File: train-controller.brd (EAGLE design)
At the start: 75.9 x 21.7 mm, 19 parts, among them IC1 MCP4131, IC2 L272, Q1 2n3906, Q2 2n2222

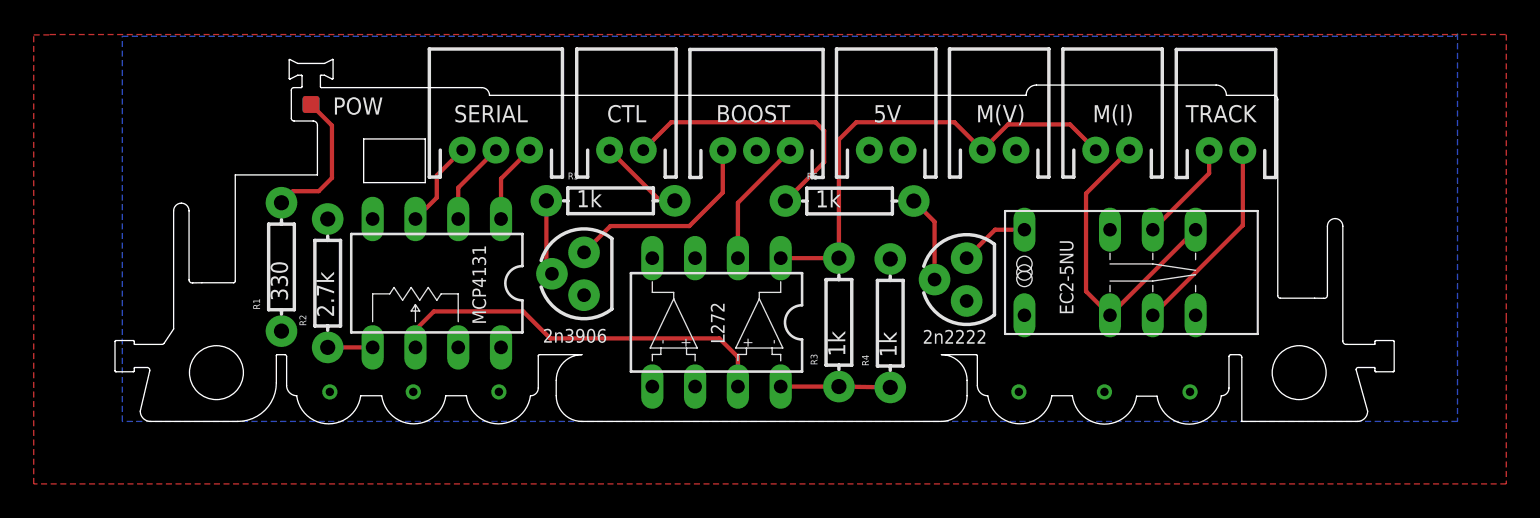
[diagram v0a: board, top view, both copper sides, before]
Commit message: board v2, adding readme and license
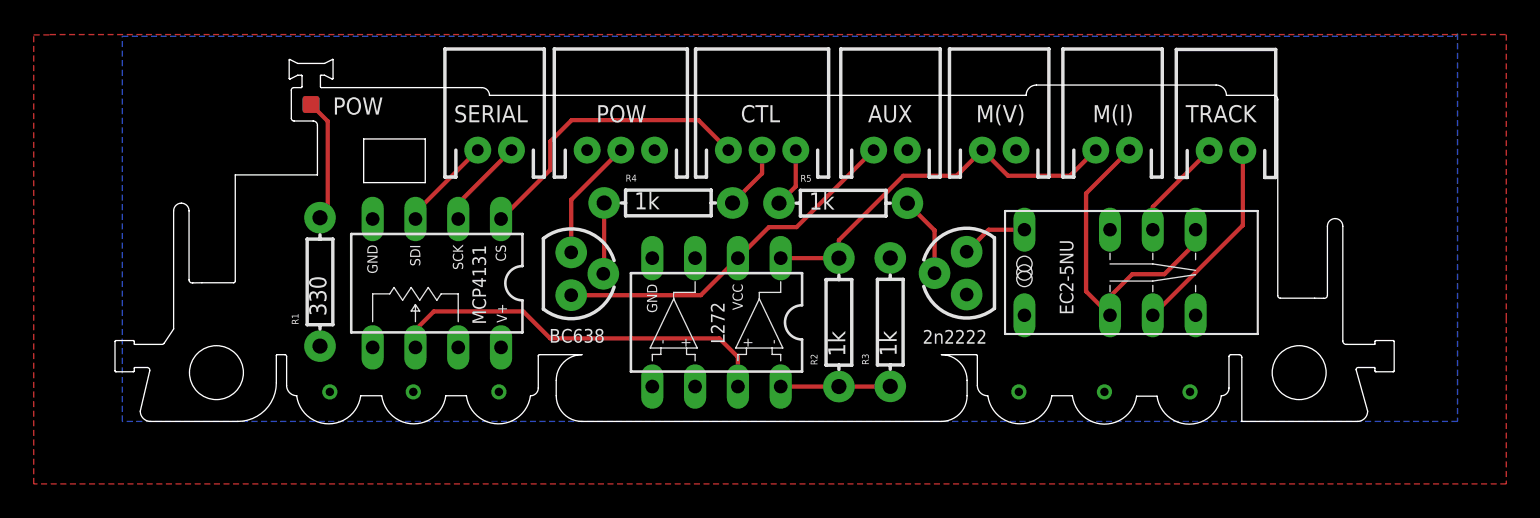
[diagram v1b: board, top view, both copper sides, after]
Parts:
- removed 5V: M02, custom-parts:JST-2-PTH
- removed BOOST: M03, custom-parts:JST-3-PTH
- removed R6: 1k, SparkFun-Resistors:AXIAL-0.3
- added AUX: M02, custom-parts:JST-2-PTH
- added POW: M03, custom-parts:JST-3-PTH
- CTL: value M02 -> M03; device custom-parts:JST-2-PTH -> custom-parts:JST-3-PTH
- Q1: value 2n3906 -> BC838
- R2: value 2.7k -> 1k
- SERIAL: value M03 -> M02; device custom-parts:JST-3-PTH -> custom-parts:JST-2-PTH
- moved R2 30.4 mm to (42.5, 6.03)
- moved R4 15.0 mm to (32.4, 13.1), turned to 0 degrees
- moved R5 13.8 mm to (42.8, 13.1)
- moved CTL 8.05 mm to (38.0, 16.3)
- moved R3 3.05 mm to (45.6, 6.05)
- moved R1 2.45 mm to (11.7, 8.43)
- moved Q1 0.76 mm to (26.6, 8.92), turned to 270 degrees
- moved Q2 0.38 mm to (50.1, 8.95)
- moved SERIAL 0.08 mm to (22.1, 16.3)
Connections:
- removed net 5V-EN: BOOST.1, Q1.3
- removed net N$2: IC1.A, R2.P$1
- new net 12V-EN: AUX.1, IC2.V+, Q1.3
- net 12V: now also POW.2, Q1.1; no longer BOOST.3, IC2.V+
- net 5V: now also IC1.B, POW.1; no longer 5V.1, Q1.1, R2.P$2
- net CS: now also CTL.1; no longer SERIAL.3
- net DIR: now also CTL.3, R5.P$1; no longer CTL.2, R6.P$1
- net EN: now also CTL.2, R4.P$2; no longer CTL.1, R5.P$2
- net GND: now also AUX.2, IC1.A, POW.3, R3.P$2; no longer 5V.2, BOOST.2, IC1.B, R4.P$2
- net N$1: now also R4.P$1; no longer R5.P$1
- net N$3: now also R2.P$1; no longer R4.P$1
- net N$6: now also R5.P$2; no longer R6.P$2
- net POW: now also R2.P$2; no longer R3.P$2
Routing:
- net 12V-EN: track 0.00 -> 21.5 mm
- net DIR: track 16.7 -> 3.56 mm
- net CS: track 4.79 -> 17.6 mm
- net 5V-EN: track 12.2 -> 0.00 mm
- net POW: track 28.1 -> 23.2 mm
- net N$2: track 2.67 -> 0.00 mm
- net EN: track 5.12 -> 3.86 mm
- net N$19: track 8.48 -> 7.32 mm
- net N$7: track 18.6 -> 19.8 mm
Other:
- board text added: "AUX"
- board text added: "BC638"
- board text removed: "2n3906"
- board text removed: "5V"
- board text removed: "BOOST"

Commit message: addressing several items from the bug/feature list
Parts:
- removed Q2: 2n2222, custom-parts:TO-92
- added D1: (no value), SparkFun-DiscreteSemi:DIODE-1N4148
- added Q3: BC638, custom-parts:TO-92
- Q1: value BC838 -> BC638
- moved POW 8.51 mm to (38.1, 16.3)
- moved CTL 8.38 mm to (29.6, 16.3)
- moved S1 1.14 mm to (60.4, 10.0)
- moved R4 0.89 mm to (31.5, 13.1)
- moved R5 0.25 mm to (42.5, 13.1)
- moved Q1 0.13 mm to (26.5, 8.92)
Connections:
- removed net N$5: Q2.3, S1.-
- new net N$2: D1.C, Q3.3, S1.+
- net 12V: now also POW.3; no longer POW.2
- net 5V: now also Q3.1; no longer S1.+
- net EN: now also R4.P$1; no longer R4.P$2
- net GND: now also D1.A, M(V).1, POW.2, S1.-; no longer M(V).2, POW.3, Q2.1
- net N$1: now also R4.P$2; no longer R4.P$1
- net N$6: now also Q3.2; no longer Q2.2
- net POW: now also M(V).2; no longer M(V).1
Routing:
- net DIR: track 3.56 -> 17.9 mm
- net CS: track 17.6 -> 6.81 mm
- net 12V: track 7.29 -> 16.1 mm
- net N$2: track 0.00 -> 8.25 mm
- net N$1: track 4.22 -> 8.92 mm
- net N$5: track 3.97 -> 0.00 mm
- net N$6: track 4.82 -> 8.25 mm
- net N$7: track 19.8 -> 18.3 mm
- net RIGHT: track 6.08 -> 4.86 mm
- net LEFT: track 12.0 -> 10.8 mm
- net 12V-EN: track 21.5 -> 22.4 mm
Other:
- board text removed: "2n2222"

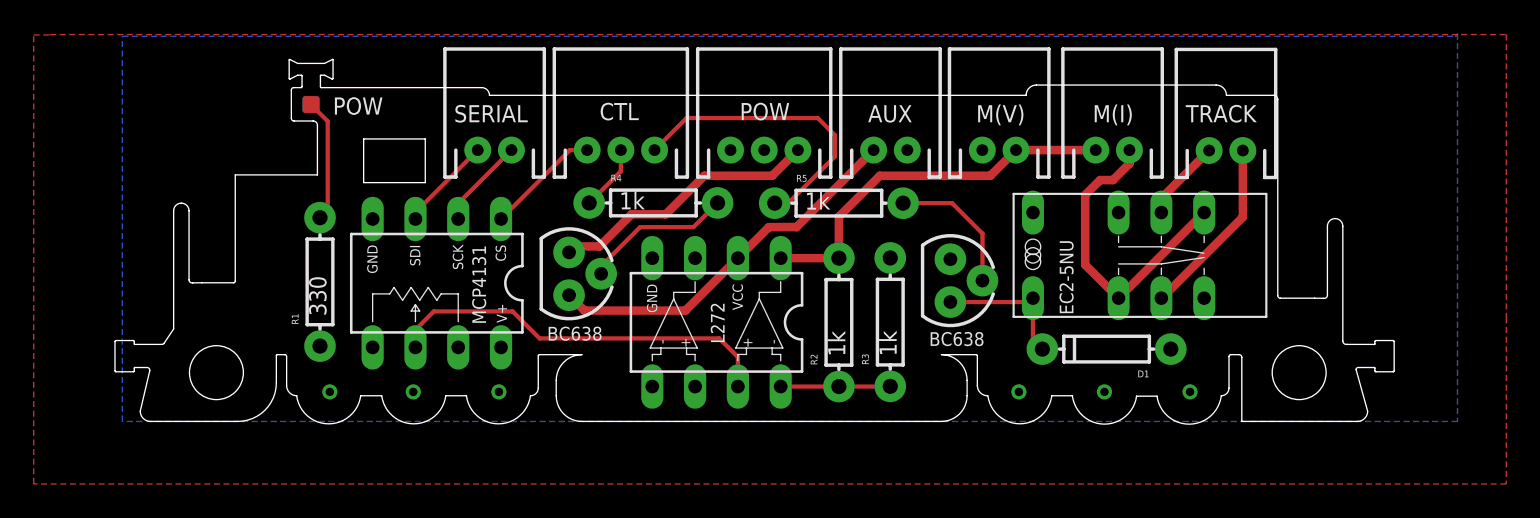
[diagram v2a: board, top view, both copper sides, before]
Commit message: adding controller board
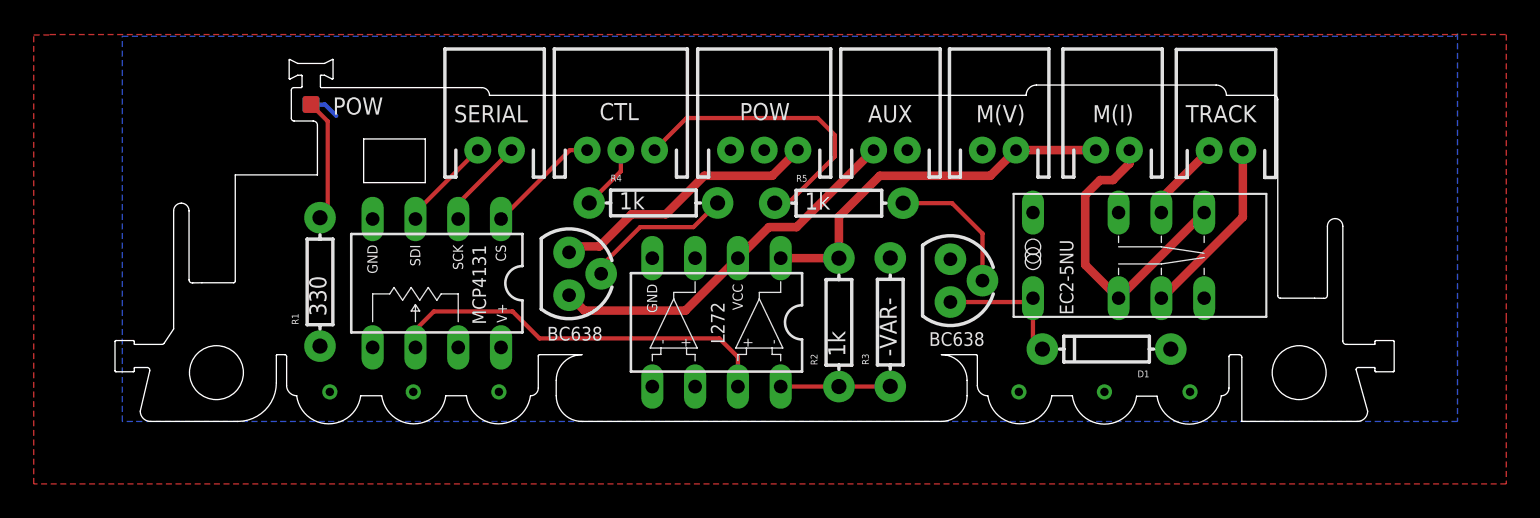
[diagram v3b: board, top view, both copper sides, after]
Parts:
- R3: value 1k -> -VAR-
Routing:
- net GND: track 0.00 -> 1.78 mm
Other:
- board text added: "Branding Goes Here V1 underdogma.net/trains"
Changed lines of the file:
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@@
 <wire x1="65.024" y1="1.7145" x2="61.595" y2="1.7145" width="0.8128" layer="30" curve="-165.227914"/>
 <wire x1="60.0075" y1="1.7145" x2="56.5785" y2="1.7145" width="0.8128" layer="30" curve="-165.227914"/>
+<text x="46.99" y="4.699" size="1.016" layer="22" rot="MR0">Branding Goes Here V1
+underdogma.net/trains</text>
 </plain>
 <attributes>
@@
 <attribute name="PROD_ID" value="RES-08380" x="86.9823" y="23.8125" size="1.778" layer="27" rot="R90" display="off"/>
 </element>
-<element name="R3" library="SparkFun-Resistors" package="AXIAL-0.3" value="1k" x="45.5803" y="6.0452" rot="R90">
+<element name="R3" library="SparkFun-Resistors" package="AXIAL-0.3" value="-VAR-" x="45.5803" y="6.0452" rot="R90">
 <attribute name="VALE" value="1k" x="90.0303" y="33.9852" size="1.778" layer="27" rot="R90" display="off"/>
 <attribute name="PROD_ID" value="RES-08380" x="90.0303" y="33.9852" size="1.778" layer="27" rot="R90" display="off"/>
@@
 <contactref element="S1" pad="-"/>
 <contactref element="D1" pad="A"/>
-<wire x1="14.859" y1="12.1666" x2="11.2014" y2="18.9618" width="0" layer="19" extent="16-16"/>
+<wire x1="11.2014" y1="18.9618" x2="12.0262" y2="18.9618" width="0.254" layer="16"/>
+<wire x1="12.0262" y1="18.9618" x2="12.7" y2="18.288" width="0.254" layer="16"/>
 </signal>
 <signal name="EN">
@@
 </board>
 </drawing>
+<compatibility>
+<note version="6.3" minversion="6.2.2" severity="warning">
+Since Version 6.2.2 text objects can contain more than one line,
+which will not be processed correctly with this version.
+</note>
+</compatibility>
 </eagle>

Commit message: getting close to final v2 board, swapping out connectors for molex kk
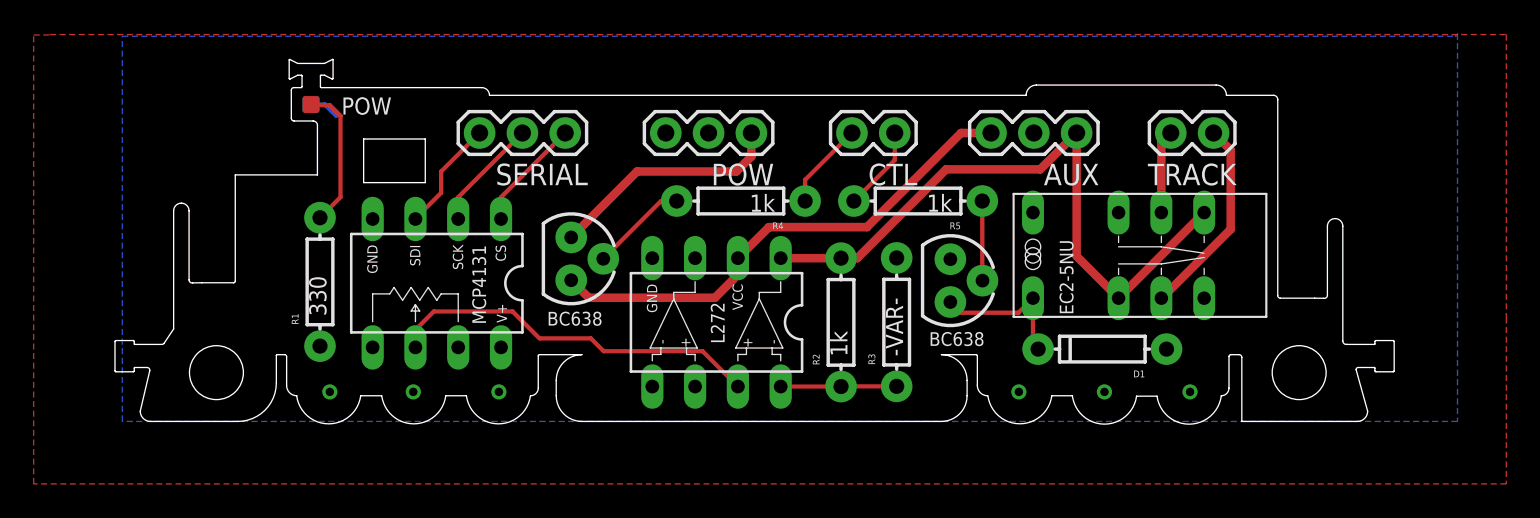
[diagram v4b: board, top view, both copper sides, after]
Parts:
- removed M(I), M(V): M02, custom-parts:JST-2-PTH
- AUX, SERIAL: value M02 -> (none); device custom-parts:JST-2-PTH -> SparkFun-Connectors:1X03
- CTL: value M03 -> (none); device custom-parts:JST-3-PTH -> SparkFun-Connectors:1X02
- POW: value M03 -> (none); device custom-parts:JST-3-PTH -> SparkFun-Connectors:1X03
- TRACK: value M02 -> (none); device custom-parts:JST-2-PTH -> SparkFun-Connectors:1X02
- moved CTL 16.3 mm to (45.8, 17.3), turned to 180 degrees
- moved AUX 11.1 mm to (56.6, 17.3), turned to 180 degrees
- moved R4 5.20 mm to (36.7, 13.2), turned to 180 degrees
- moved R5 4.70 mm to (47.2, 13.2), turned to 180 degrees
- moved SERIAL 4.31 mm to (26.3, 17.3), turned to 180 degrees
- moved TRACK 1.28 mm to (64.8, 17.3), turned to 180 degrees
- moved POW 1.27 mm to (37.3, 17.3), turned to 180 degrees
- moved Q1 0.90 mm to (26.6, 9.80)
- moved R3 0.38 mm to (46.0, 6.05)
- moved D1 0.25 mm to (58.2, 4.45)
- moved R2 0.13 mm to (42.7, 6.03)
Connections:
- removed net N$6: Q3.2, R5.P$2
- removed net N$7: M(I).2, S1.NC1, S1.NO2
- new net N$5: Q3.2, R5.P$1
- net 12V: now also POW.1; no longer POW.3
- net 12V-EN: now also AUX.3; no longer AUX.1
- net 5V: now also POW.3; no longer POW.1
- net CS: now also SERIAL.1; no longer CTL.1
- net DIR: now also CTL.1, R5.P$2; no longer CTL.3, R5.P$1
- net GND: no longer M(V).1
- net LEFT: now also TRACK.1; no longer TRACK.2
- net POW: now also AUX.1, S1.NC1, S1.NO2; no longer M(I).1, M(V).2
- net RIGHT: now also TRACK.2; no longer TRACK.1
- net SDI: now also SERIAL.3; no longer SERIAL.1
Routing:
- net N$7: track 18.3 -> 0.00 mm
- net POW: track 22.8 -> 38.7 mm
- net DIR: track 17.9 -> 5.04 mm
- net N$6: track 8.25 -> 0.00 mm
- net 12V-EN: track 22.4 -> 30.0 mm
- net N$5: track 0.00 -> 4.73 mm
- net N$1: track 8.92 -> 5.78 mm
- net 12V: track 16.1 -> 14.1 mm
- net SCK: track 5.40 -> 6.68 mm
- net EN: track 3.92 -> 5.19 mm
- net N$19: track 7.32 -> 8.58 mm
- net LEFT: track 10.8 -> 11.9 mm
- net SDI: track 5.62 -> 6.68 mm
- net WIPER: track 23.5 -> 22.5 mm
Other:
- board text removed: "AUX"
- board text removed: "CTL"
- board text removed: "M(I)"
- board text removed: "M(V)"
- board text removed: "SERIAL"
- board text removed: "TRACK"
